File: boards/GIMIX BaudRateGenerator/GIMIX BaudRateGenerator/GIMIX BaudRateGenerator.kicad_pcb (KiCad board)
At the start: 2 copper layers, 58.4 x 83.8 mm, 19 parts, among them J1 Mainboard, J2 Conn_01x05, J3 Range, J4 A, J5 B, J6 C, J7 D, J8 E, J9 Conn_02x05_Odd_Even, U1 MC14411, U2 4512, U3 4069, U4 74LS244, Y1 1M8324

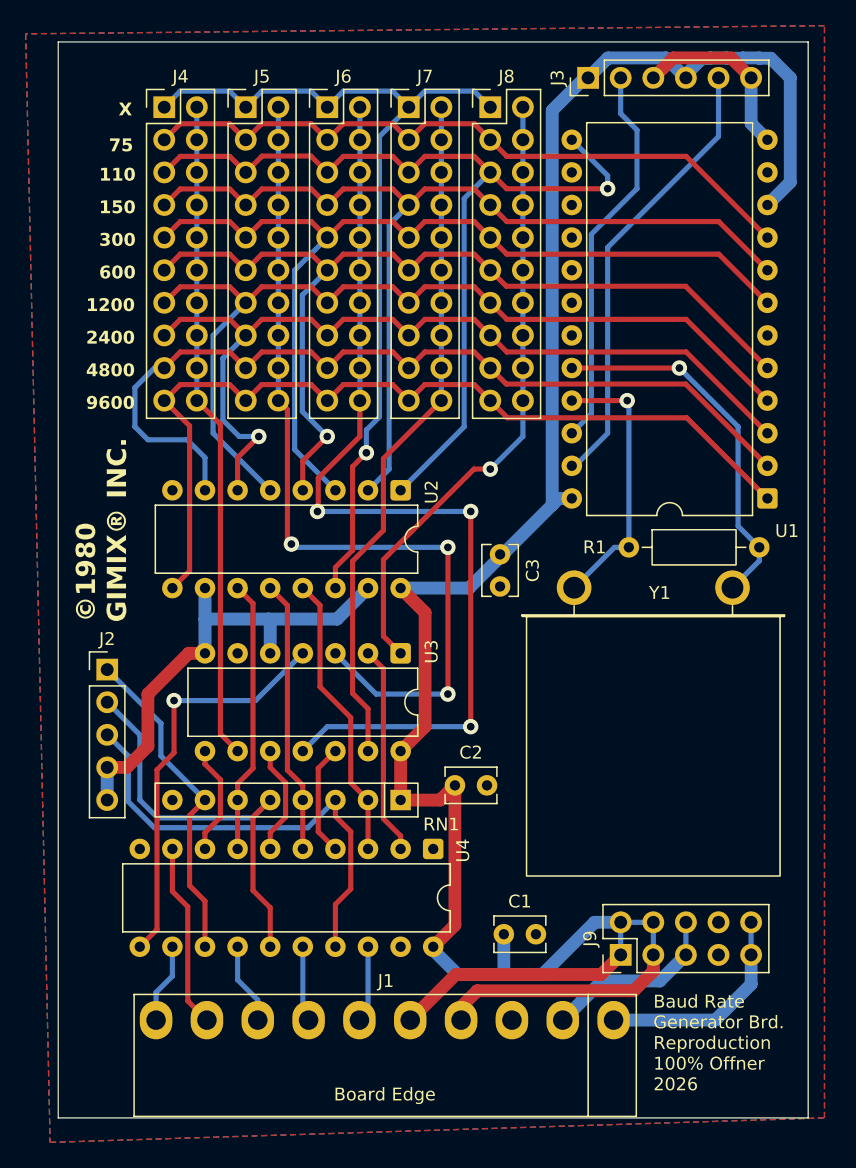
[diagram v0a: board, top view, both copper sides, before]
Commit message: Baudrate Gen. silkscreen and gerbers added
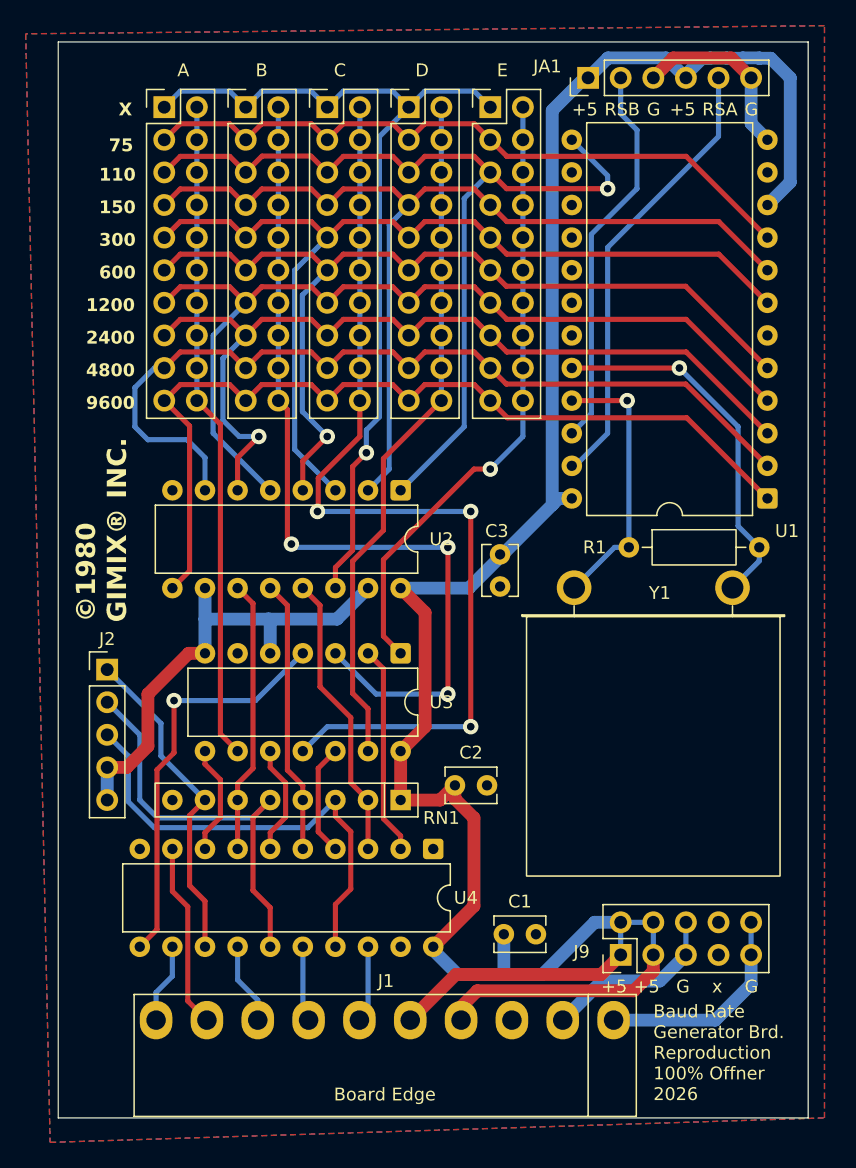
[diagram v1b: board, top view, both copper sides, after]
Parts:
- renumbered J3 to JA1
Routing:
- net +5V: track 181.0 -> 182.3 mm
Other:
- board text added: "+5"
- board text added: "A"
- board text added: "B"
- board text added: "C"
- board text added: "D"
- board text added: "E"
- board text added: "G"
- board text added: "RSA"
- board text added: "RSB"
- board text added: "x"
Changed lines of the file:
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@@
 			(outputformat 1)
 			(mirror no)
-			(drillshape 1)
+			(drillshape 0)
 			(scaleselection 1)
-			(outputdirectory "")
+			(outputdirectory "baudrate_gen")
 		)
 	)
@@
 	(net 9 "/PU3")
 	(net 10 "/PU5")
-	(net 11 "Net-(J3-Pin_5)")
-	(net 12 "Net-(J3-Pin_2)")
+	(net 11 "Net-(JA1-Pin_5)")
+	(net 12 "Net-(JA1-Pin_2)")
 	(net 13 "/F1")
 	(net 14 "/F9")
@@
 		(tags "THT DIP DIL PDIP 2.54mm 7.62mm 300mil")
 		(property "Reference" "U3"
-			(at -0.127 -2.413 90)
+			(at 3.81 -3.175 180)
 			(layer "F.SilkS")
 			(effects
@@
 			(at 1.27 -2.38 0)
 			(layer "F.SilkS")
+			(hide yes)
 			(effects
 				(font
@@
 			(at 1.27 -2.38 0)
 			(layer "F.SilkS")
+			(hide yes)
 			(effects
 				(font
@@
 			(layers "*.Cu" "*.Mask")
 			(remove_unused_layers no)
-			(net 12 "Net-(J3-Pin_2)")
+			(net 12 "Net-(JA1-Pin_2)")
 			(pinfunction "RSELb")
 			(pintype "input")
@@
 			(layers "*.Cu" "*.Mask")
 			(remove_unused_layers no)
-			(net 11 "Net-(J3-Pin_5)")
+			(net 11 "Net-(JA1-Pin_5)")
 			(pinfunction "RSELa")
 			(pintype "input")
@@
 		(tags "Through hole pin header THT 2x05 2.54mm double row")
 		(property "Reference" "J9"
-			(at 1.27 -2.38 90)
+			(at 0.254 -3.048 180)
 			(layer "F.SilkS")
 			(effects
@@
 		(tags "THT DIP DIL PDIP 2.54mm 7.62mm 300mil")
 		(property "Reference" "U4"
-			(at 0.127 -2.33 90)
+			(at 3.81 -2.54 180)
 			(layer "F.SilkS")
 			(effects
@@
 		(tags "R")
 		(property "Reference" "RN1"
-			(at -3.175 -1.905 0)
+			(at -3.175 -1.397 0)
 			(layer "F.SilkS")
 			(effects
@@
 			(at 1.27 -2.38 0)
 			(layer "F.SilkS")
+			(hide yes)
 			(effects
 				(font
@@
 		(tags "THT DIP DIL PDIP 2.54mm 7.62mm 300mil")
 		(property "Reference" "U2"
-			(at 0.127 -2.413 90)
+			(at 3.81 -3.175 180)
 			(layer "F.SilkS")
 			(effects
@@
 			(at 1.27 -2.38 0)
 			(layer "F.SilkS")
+			(hide yes)
 			(effects
 				(font
@@
 		(tags "C Disc series Radial pin pitch 2.50mm diameter 3.8mm width 2.6mm Capacitor")
 		(property "Reference" "C3"
-			(at 1.25 -2.55 90)
+			(at -1.818 0.254 180)
 			(layer "F.SilkS")
 			(effects
@@
 		(descr "Through hole straight pin header, 1x06, 2.54mm pitch, single row")
 		(tags "Through hole pin header THT 1x06 2.54mm single row")
-		(property "Reference" "J3"
-			(at 0 -2.38 90)
+		(property "Reference" "JA1"
+			(at 0.889 -3.175 180)
 			(layer "F.SilkS")
 			(effects
@@
 			(layers "*.Cu" "*.Mask")
 			(remove_unused_layers no)
-			(net 12 "Net-(J3-Pin_2)")
+			(net 12 "Net-(JA1-Pin_2)")
 			(pinfunction "Pin_2")
 			(pintype "passive")
@@
 			(layers "*.Cu" "*.Mask")
 			(remove_unused_layers no)
-			(net 11 "Net-(J3-Pin_5)")
+			(net 11 "Net-(JA1-Pin_5)")
 			(pinfunction "Pin_5")
 			(pintype "passive")
@@
 			(at 1.27 -2.38 0)
 			(layer "F.SilkS")
+			(hide yes)
 			(effects
 				(font
@@
 		)
 	)
+	(gr_text "A"
+		(at 145.796 71.374 0)
+		(layer "F.SilkS")
+		(effects
+			(font
+				(size 1 1)
+				(thickness 0.15)
+			)
+			(justify left bottom)
+		)
+	)
+	(gr_text "B"
+		(at 151.892 71.374 0)
+		(layer "F.SilkS")
+		(effects
+			(font
+				(size 1 1)
+				(thickness 0.15)
+			)
+			(justify left bottom)
+		)
+	)
+	(gr_text "C"
+		(at 157.988 71.374 0)
+		(layer "F.SilkS")
+		(effects
+			(font
+				(size 1 1)
+				(thickness 0.15)
+			)
+			(justify left bottom)
+		)
+	)
+	(gr_text "D"
+		(at 164.338 71.374 0)
+		(layer "F.SilkS")
+		(effects
+			(font
+				(size 1 1)
+				(thickness 0.15)
+			)
+			(justify left bottom)
+		)
+	)
+	(gr_text "E"
+		(at 170.688 71.374 0)
+		(layer "F.SilkS")
+		(effects
+			(font
+				(size 1 1)
+				(thickness 0.15)
+			)
+			(justify left bottom)
+		)
+	)
+	(gr_text "+5"
+		(at 176.53 74.422 0)
+		(layer "F.SilkS")
+		(effects
+			(font
+				(size 1 1)
+				(thickness 0.15)
+			)
+			(justify left bottom)
+		)
+	)
+	(gr_text "+5"
+		(at 178.816 142.748 0)
+		(layer "F.SilkS")
+		(effects
+			(font
+				(size 1 1)
+				(thickness 0.15)
+			)
+			(justify left bottom)
+		)
+	)
+	(gr_text "RSB"
+		(at 179.07 74.422 0)
+		(layer "F.SilkS")
+		(effects
+			(font
+				(size 1 1)
+				(thickness 0.15)
+			)
+			(justify left bottom)
+		)
+	)
+	(gr_text "+5"
+		(at 181.356 142.748 0)
+		(layer "F.SilkS")
+		(effects
+			(font
+				(size 1 1)
+				(thickness 0.15)
+			)
+			(justify left bottom)
+		)
+	)
+	(gr_text "G"
+		(at 182.372 74.422 0)
+		(layer "F.SilkS")
+		(effects
+			(font
+				(size 1 1)
+				(thickness 0.15)
+			)
+			(justify left bottom)
+		)
+	)
 	(gr_text "Baud Rate \nGenerator Brd.\nReproduction\n100% Offner \n2026"
-		(at 182.88 150.368 0)
+		(at 182.88 151.13 0)
+		(layer "F.SilkS")
+		(effects
+			(font
+				(size 1 1)
+				(thickness 0.15)
+			)
+			(justify left bottom)
+		)
+	)
+	(gr_text "+5"
+		(at 184.15 74.422 0)
+		(layer "F.SilkS")
+		(effects
+			(font
+				(size 1 1)
+				(thickness 0.15)
+			)
+			(justify left bottom)
+		)
+	)
+	(gr_text "G"
+		(at 184.658 142.748 0)
+		(layer "F.SilkS")
+		(effects
+			(font
+				(size 1 1)
+				(thickness 0.15)
+			)
+			(justify left bottom)
+		)
+	)
+	(gr_text "RSA"
+		(at 186.69 74.422 0)
+		(layer "F.SilkS")
+		(effects
+			(font
+				(size 1 1)
+				(thickness 0.15)
+			)
+			(justify left bottom)
+		)
+	)
+	(gr_text "x"
+		(at 187.452 142.748 0)
 		(layer "F.SilkS")
 		(effects
 			(font
 				(size 1 1)
-				(thickness 0.1)
+				(thickness 0.15)
+			)
+			(justify left bottom)
+		)
+	)
+	(gr_text "G"
+		(at 189.992 74.422 0)
+		(layer "F.SilkS")
+		(effects
+			(font
+				(size 1 1)
+				(thickness 0.15)
+			)
+			(justify left bottom)
+		)
+	)
+	(gr_text "G"
+		(at 189.992 142.748 0)
+		(layer "F.SilkS")
+		(effects
+			(font
+				(size 1 1)
+				(thickness 0.15)
 			)
 			(justify left bottom)
@@
 	)
 	(segment
-		(start 167.426 137.374)
-		(end 167.426 126.492)
-		(width 1)
-		(layer "F.Cu")
-		(net 4)
-	)
-	(segment
 		(start 181.356 142.494)
 		(end 182.88 140.97)
@@
 	(segment
 		(start 165.735 139.065)
-		(end 167.426 137.374)
+		(end 168.91 135.89)
 		(width 1)
 		(layer "F.Cu")
@@
 	)
 	(segment
+		(start 168.91 135.89)
+		(end 168.91 129.032)
+		(width 1)
+		(layer "F.Cu")
+		(net 4)
+	)
+	(segment
+		(start 168.91 129.032)
+		(end 167.426 127.548)
+		(width 1)
+		(layer "F.Cu")
+		(net 4)
+	)
+	(segment
 		(start 166.283 127.635)
 		(end 167.426 126.492)
@@
 		(width 1)
 		(layer "F.Cu")
+		(net 4)
+	)
+	(segment
+		(start 167.426 127.548)
+		(end 167.426 126.492)
+		(width 1)
+		(layer "F.Cu")
